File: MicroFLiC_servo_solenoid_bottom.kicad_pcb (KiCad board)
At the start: 2 copper layers, 49.8 x 49.8 mm, 37 parts, among them P1 1x14 header strip, P10 1x4 socket strip, P11 2x3 header strip R/A, P12 2x3 header strip R/A, P2 1x14 socket strip, P3 12-way Micro-MaTch, P4 Jack_3.5mm_3pin, P5 Jack_3.5mm_3pin, P6 RCA_3, P7 RCA_3, P8 1x6 socket strip, P9 1x4 header strip, U1 PCA9306DP, U2 DRV103, U3 DRV103, U4 MCP4728

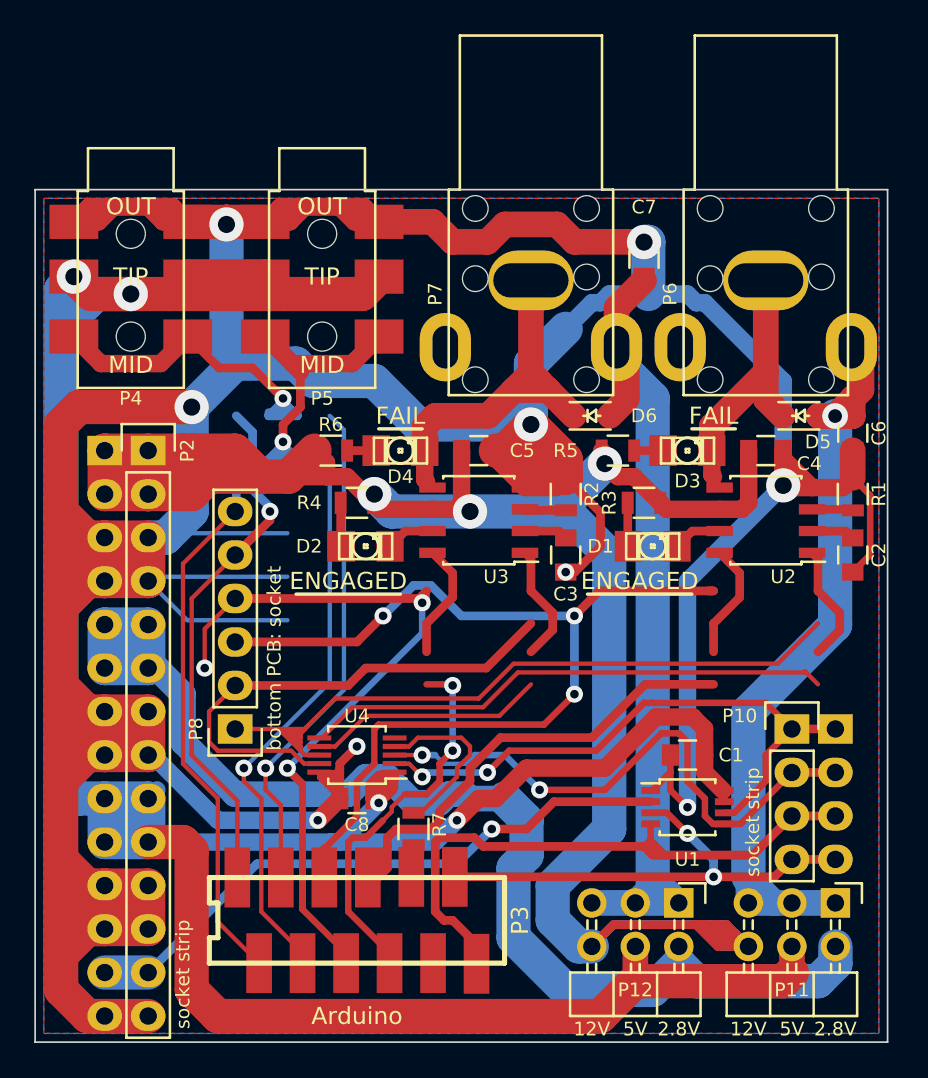
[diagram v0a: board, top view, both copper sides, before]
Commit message: Fixed PCB routing
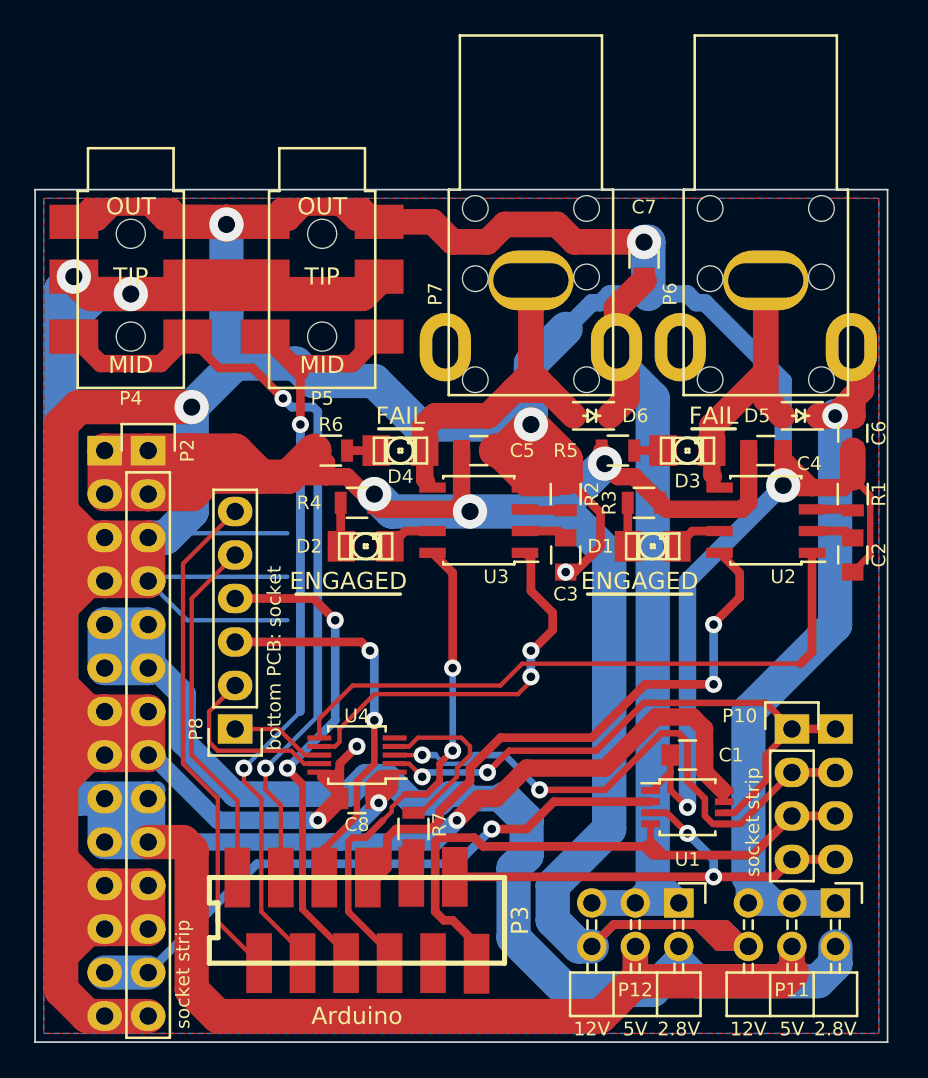
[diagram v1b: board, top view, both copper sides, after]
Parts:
- turned D5 to 180 degrees
- turned D6 to 180 degrees
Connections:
- P3 pad 10: Net-(P3-Pad10) -> (no net)
- P6 pad 3: Net-(P6-Pad3) -> (no net)
- P7 pad 3: Net-(P7-Pad3) -> (no net)
- U4 pad 5: Net-(U4-Pad5) -> (no net)
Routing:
- net /shutterPWM/SH3_PWM: track 45.7 -> 5.54 mm
- net /SH3: track 59.6 -> 24.3 mm, vias 3 -> 2
- net /shutterPWM/SH4_PWM: track 29.7 -> 10.9 mm
- net /SH4: track 51.5 -> 37.8 mm, vias 3 -> 2
- net /shutterPWM/SHB_O/C: track 10.6 -> 23.2 mm
- net /shutterPWM/SHB_PWR: track 61.8 -> 49.2 mm
- net /SERVO3: track 30.8 -> 21.0 mm, vias 1 -> 0
- net /SERVO2: track 51.7 -> 46.0 mm
- net /SERVO1: track 50.6 -> 46.8 mm
- net /SERVO4: track 32.6 -> 29.6 mm
- net /shutterPWM/SH2_PWM: track 20.8 -> 23.2 mm, vias 0 -> 2
- net /shutterPWM/SH1: track 38.5 -> 40.4 mm, vias 0 -> 2
- net /shutterPWM/SH2: track 30.5 -> 31.9 mm
- net /shutterPWM/SH1_PWM: track 38.2 -> 37.5 mm
